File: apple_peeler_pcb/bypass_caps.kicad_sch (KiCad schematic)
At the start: 16 parts

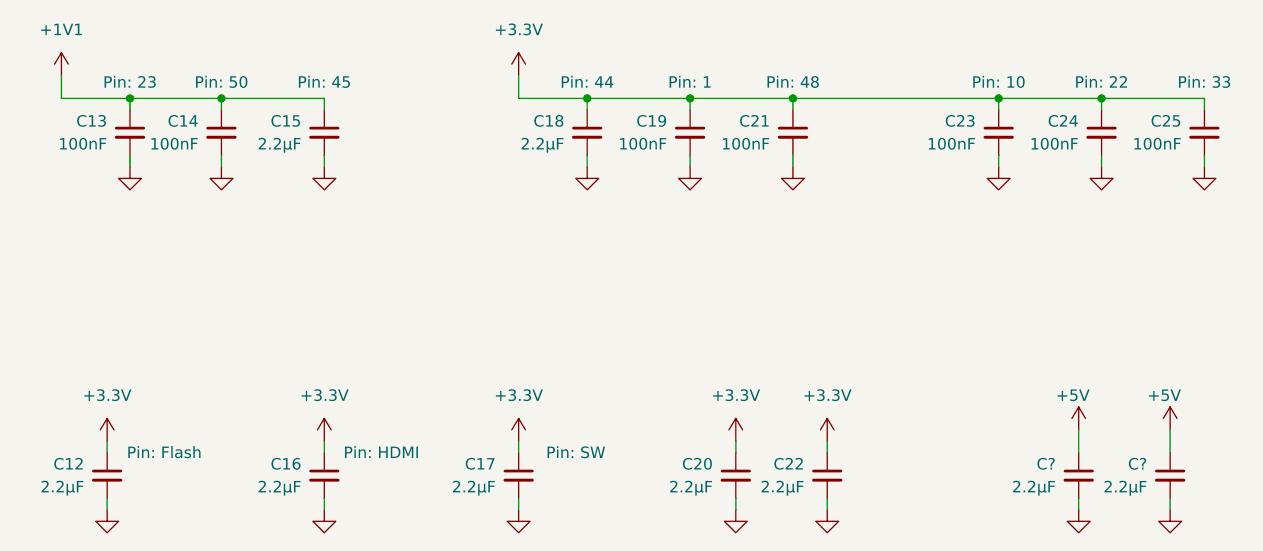
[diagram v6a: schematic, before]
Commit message: all components placed inside board
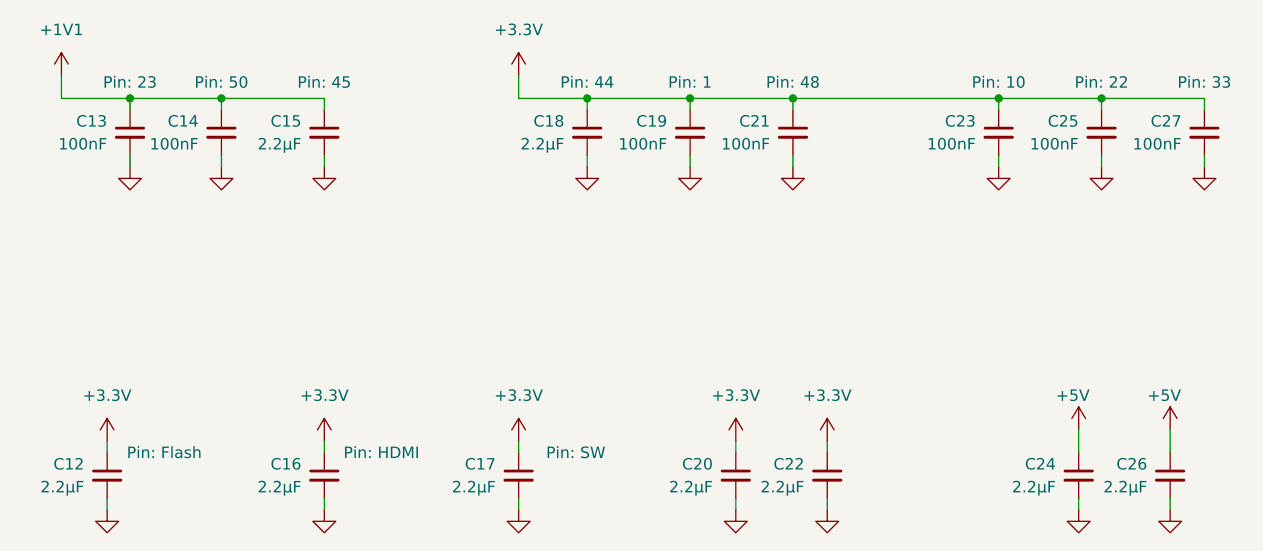
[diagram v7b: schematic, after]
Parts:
- gave numbers to parts that had none: 2
- renumbered C24 to C25, C25 to C27
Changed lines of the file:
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@@
 		(dnp no)
 		(fields_autoplaced yes)
-		(property "Reference" "#PWR086"
+		(property "Reference" "#PWR087"
 			(at 161.29 111.76 0)
 			(effects
@@
 			(project "apple_peeler_pcb"
 				(path "/d5946b96-44a8-4a28-8641-19803e1510af/36c29319-2fb9-4e97-8e03-94576ed291d6"
-					(reference "#PWR086")
+					(reference "#PWR087")
 					(unit 1)
 				)
@@
 		(dnp no)
 		(fields_autoplaced yes)
-		(property "Reference" "#PWR083"
+		(property "Reference" "#PWR084"
 			(at 151.13 111.76 0)
 			(effects
@@
 			(project "apple_peeler_pcb"
 				(path "/d5946b96-44a8-4a28-8641-19803e1510af/36c29319-2fb9-4e97-8e03-94576ed291d6"
-					(reference "#PWR083")
+					(reference "#PWR084")
 					(unit 1)
 				)
@@
 		(dnp no)
 		(fields_autoplaced yes)
-		(property "Reference" "#PWR081"
+		(property "Reference" "#PWR082"
 			(at 146.05 73.66 0)
 			(effects
@@
 			(project ""
 				(path "/d5946b96-44a8-4a28-8641-19803e1510af/36c29319-2fb9-4e97-8e03-94576ed291d6"
-					(reference "#PWR081")
+					(reference "#PWR082")
 					(unit 1)
 				)
@@
 		(dnp no)
 		(fields_autoplaced yes)
-		(property "Reference" "#PWR079"
+		(property "Reference" "#PWR080"
 			(at 127 111.76 0)
 			(effects
@@
 			(project "apple_peeler_pcb"
 				(path "/d5946b96-44a8-4a28-8641-19803e1510af/36c29319-2fb9-4e97-8e03-94576ed291d6"
-					(reference "#PWR079")
+					(reference "#PWR080")
 					(unit 1)
 				)
@@
 		(dnp no)
 		(fields_autoplaced yes)
-		(property "Reference" "#PWR0126"
+		(property "Reference" "#PWR093"
 			(at 199.39 111.76 0)
 			(effects
@@
 			(project "apple_peeler_pcb"
 				(path "/d5946b96-44a8-4a28-8641-19803e1510af/36c29319-2fb9-4e97-8e03-94576ed291d6"
-					(reference "#PWR0126")
+					(reference "#PWR093")
 					(unit 1)
 				)
@@
 		(dnp no)
 		(fields_autoplaced yes)
-		(property "Reference" "#PWR074"
+		(property "Reference" "#PWR075"
 			(at 105.41 73.66 0)
 			(effects
@@
 			(project ""
 				(path "/d5946b96-44a8-4a28-8641-19803e1510af/36c29319-2fb9-4e97-8e03-94576ed291d6"
-					(reference "#PWR074")
+					(reference "#PWR075")
 					(unit 1)
 				)
@@
 		(dnp no)
 		(fields_autoplaced yes)
-		(property "Reference" "#PWR080"
+		(property "Reference" "#PWR081"
 			(at 134.62 73.66 0)
 			(effects
@@
 			(project ""
 				(path "/d5946b96-44a8-4a28-8641-19803e1510af/36c29319-2fb9-4e97-8e03-94576ed291d6"
-					(reference "#PWR080")
+					(reference "#PWR081")
 					(unit 1)
 				)
@@
 		(dnp no)
 		(fields_autoplaced yes)
-		(property "Reference" "#PWR069"
+		(property "Reference" "#PWR070"
 			(at 76.2 60.96 0)
 			(effects
@@
 			(project ""
 				(path "/d5946b96-44a8-4a28-8641-19803e1510af/36c29319-2fb9-4e97-8e03-94576ed291d6"
-					(reference "#PWR069")
+					(reference "#PWR070")
 					(unit 1)
 				)
@@
 		(dnp no)
 		(fields_autoplaced yes)
-		(property "Reference" "#PWR077"
+		(property "Reference" "#PWR078"
 			(at 127 60.96 0)
 			(effects
@@
 			(project ""
 				(path "/d5946b96-44a8-4a28-8641-19803e1510af/36c29319-2fb9-4e97-8e03-94576ed291d6"
-					(reference "#PWR077")
+					(reference "#PWR078")
 					(unit 1)
 				)
@@
 		(dnp no)
 		(fields_autoplaced yes)
-		(property "Reference" "#PWR089"
+		(property "Reference" "#PWR094"
 			(at 203.2 73.66 0)
 			(effects
@@
 			(project ""
 				(path "/d5946b96-44a8-4a28-8641-19803e1510af/36c29319-2fb9-4e97-8e03-94576ed291d6"
-					(reference "#PWR089")
+					(reference "#PWR094")
 					(unit 1)
 				)
@@
 		(dnp no)
 		(fields_autoplaced yes)
-		(property "Reference" "#PWR072"
+		(property "Reference" "#PWR073"
 			(at 83.82 73.66 0)
 			(effects
@@
 			(project ""
 				(path "/d5946b96-44a8-4a28-8641-19803e1510af/36c29319-2fb9-4e97-8e03-94576ed291d6"
-					(reference "#PWR072")
+					(reference "#PWR073")
 					(unit 1)
 				)
@@
 		(on_board yes)
 		(dnp no)
-		(property "Reference" "#PWR0123"
+		(property "Reference" "#PWR089"
 			(at 189.23 100.33 0)
 			(effects
@@
 			(project "apple_peeler_pcb"
 				(path "/d5946b96-44a8-4a28-8641-19803e1510af/36c29319-2fb9-4e97-8e03-94576ed291d6"
-					(reference "#PWR0123")
+					(reference "#PWR089")
 					(unit 1)
 				)
@@
 		(dnp no)
 		(fields_autoplaced yes)
-		(property "Reference" "#PWR073"
+		(property "Reference" "#PWR074"
 			(at 93.98 73.66 0)
 			(effects
@@
 			(project ""
 				(path "/d5946b96-44a8-4a28-8641-19803e1510af/36c29319-2fb9-4e97-8e03-94576ed291d6"
-					(reference "#PWR073")
+					(reference "#PWR074")
 					(unit 1)
 				)
@@
 		(on_board yes)
 		(dnp no)
-		(property "Reference" "C24"
+		(property "Reference" "C25"
 			(at 189.23 62.2362 0)
 			(effects
@@
 			(project ""
 				(path "/d5946b96-44a8-4a28-8641-19803e1510af/36c29319-2fb9-4e97-8e03-94576ed291d6"
-					(reference "C24")
+					(reference "C25")
 					(unit 1)
 				)
@@
 		(dnp no)
 		(fields_autoplaced yes)
-		(property "Reference" "#PWR084"
+		(property "Reference" "#PWR085"
 			(at 157.48 73.66 0)
 			(effects
@@
 			(project ""
 				(path "/d5946b96-44a8-4a28-8641-19803e1510af/36c29319-2fb9-4e97-8e03-94576ed291d6"
-					(reference "#PWR084")
+					(reference "#PWR085")
 					(unit 1)
 				)
@@
 		(on_board yes)
 		(dnp no)
-		(property "Reference" "C?"
+		(property "Reference" "C24"
 			(at 186.69 100.3362 0)
 			(effects
@@
 			(project "apple_peeler_pcb"
 				(path "/d5946b96-44a8-4a28-8641-19803e1510af/36c29319-2fb9-4e97-8e03-94576ed291d6"
-					(reference "C?")
+					(reference "C24")
 					(unit 1)
 				)
@@
 		(dnp no)
 		(fields_autoplaced yes)
-		(property "Reference" "#PWR070"
+		(property "Reference" "#PWR071"
 			(at 81.28 101.6 0)
 			(effects
@@
 			(project "apple_peeler_pcb"
 				(path "/d5946b96-44a8-4a28-8641-19803e1510af/36c29319-2fb9-4e97-8e03-94576ed291d6"
-					(reference "#PWR070")
+					(reference "#PWR071")
 					(unit 1)
 				)
@@
 		(dnp no)
 		(fields_autoplaced yes)
-		(property "Reference" "#PWR087"
+		(property "Reference" "#PWR088"
 			(at 180.34 73.66 0)
 			(effects
@@
 			(project ""
 				(path "/d5946b96-44a8-4a28-8641-19803e1510af/36c29319-2fb9-4e97-8e03-94576ed291d6"
-					(reference "#PWR087")
+					(reference "#PWR088")
 					(unit 1)
 				)
@@
 		(on_board yes)
 		(dnp no)
-		(property "Reference" "C25"
+		(property "Reference" "C27"
 			(at 200.66 62.2362 0)
 			(effects
@@
 			(project ""
 				(path "/d5946b96-44a8-4a28-8641-19803e1510af/36c29319-2fb9-4e97-8e03-94576ed291d6"
-					(reference "C25")
+					(reference "C27")
 					(unit 1)
 				)
@@
 		(dnp no)
 		(fields_autoplaced yes)
-		(property "Reference" "#PWR075"
+		(property "Reference" "#PWR076"
 			(at 105.41 101.6 0)
 			(effects
@@
 			(project "apple_peeler_pcb"
 				(path "/d5946b96-44a8-4a28-8641-19803e1510af/36c29319-2fb9-4e97-8e03-94576ed291d6"
-					(reference "#PWR075")
+					(reference "#PWR076")
 					(unit 1)
 				)
@@
 		(dnp no)
 		(fields_autoplaced yes)
-		(property "Reference" "#PWR071"
+		(property "Reference" "#PWR072"
 			(at 81.28 111.76 0)
 			(effects
@@
 			(project "apple_peeler_pcb"
 				(path "/d5946b96-44a8-4a28-8641-19803e1510af/36c29319-2fb9-4e97-8e03-94576ed291d6"
-					(reference "#PWR071")
+					(reference "#PWR072")
 					(unit 1)
 				)
@@
 		(dnp no)
 		(fields_autoplaced yes)
-		(property "Reference" "#PWR078"
+		(property "Reference" "#PWR079"
 			(at 127 101.6 0)
 			(effects
@@
 			(project "apple_peeler_pcb"
 				(path "/d5946b96-44a8-4a28-8641-19803e1510af/36c29319-2fb9-4e97-8e03-94576ed291d6"
-					(reference "#PWR078")
+					(reference "#PWR079")
 					(unit 1)
 				)
@@
 		(dnp no)
 		(fields_autoplaced yes)
-		(property "Reference" "#PWR088"
+		(property "Reference" "#PWR091"
 			(at 191.77 73.66 0)
 			(effects
@@
 			(project ""
 				(path "/d5946b96-44a8-4a28-8641-19803e1510af/36c29319-2fb9-4e97-8e03-94576ed291d6"
-					(reference "#PWR088")
+					(reference "#PWR091")
 					(unit 1)
 				)
@@
 		(on_board yes)
 		(dnp no)
-		(property "Reference" "C?"
+		(property "Reference" "C26"
 			(at 196.85 100.3362 0)
 			(effects
@@
 			(project "apple_peeler_pcb"
 				(path "/d5946b96-44a8-4a28-8641-19803e1510af/36c29319-2fb9-4e97-8e03-94576ed291d6"
-					(reference "C?")
+					(reference "C26")
 					(unit 1)
 				)
@@
 		(dnp no)
 		(fields_autoplaced yes)
-		(property "Reference" "#PWR0124"
+		(property "Reference" "#PWR090"
 			(at 189.23 111.76 0)
 			(effects
@@
 			(project "apple_peeler_pcb"
 				(path "/d5946b96-44a8-4a28-8641-19803e1510af/36c29319-2fb9-4e97-8e03-94576ed291d6"
-					(reference "#PWR0124")
+					(reference "#PWR090")
 					(unit 1)
 				)
@@
 		(dnp no)
 		(fields_autoplaced yes)
-		(property "Reference" "#PWR085"
+		(property "Reference" "#PWR086"
 			(at 161.29 101.6 0)
 			(effects
@@
 			(project "apple_peeler_pcb"
 				(path "/d5946b96-44a8-4a28-8641-19803e1510af/36c29319-2fb9-4e97-8e03-94576ed291d6"
-					(reference "#PWR085")
+					(reference "#PWR086")
 					(unit 1)
 				)
@@
 		(dnp no)
 		(fields_autoplaced yes)
-		(property "Reference" "#PWR076"
+		(property "Reference" "#PWR077"
 			(at 105.41 111.76 0)
 			(effects
@@
 			(project "apple_peeler_pcb"
 				(path "/d5946b96-44a8-4a28-8641-19803e1510af/36c29319-2fb9-4e97-8e03-94576ed291d6"
-					(reference "#PWR076")
+					(reference "#PWR077")
 					(unit 1)
 				)
@@
 		(dnp no)
 		(fields_autoplaced yes)
-		(property "Reference" "#PWR082"
+		(property "Reference" "#PWR083"
 			(at 151.13 101.6 0)
 			(effects
@@
 			(project "apple_peeler_pcb"
 				(path "/d5946b96-44a8-4a28-8641-19803e1510af/36c29319-2fb9-4e97-8e03-94576ed291d6"
-					(reference "#PWR082")
+					(reference "#PWR083")
 					(unit 1)
 				)
@@
 		(on_board yes)
 		(dnp no)
-		(property "Reference" "#PWR0125"
+		(property "Reference" "#PWR092"
 			(at 199.39 100.33 0)
 			(effects
@@
 			(project "apple_peeler_pcb"
 				(path "/d5946b96-44a8-4a28-8641-19803e1510af/36c29319-2fb9-4e97-8e03-94576ed291d6"
-					(reference "#PWR0125")
-					(unit 1)
-				)
+					(reference "#PWR092")
+					(unit 1)
+				)

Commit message: copper seems done, only thing left is the silkscreen
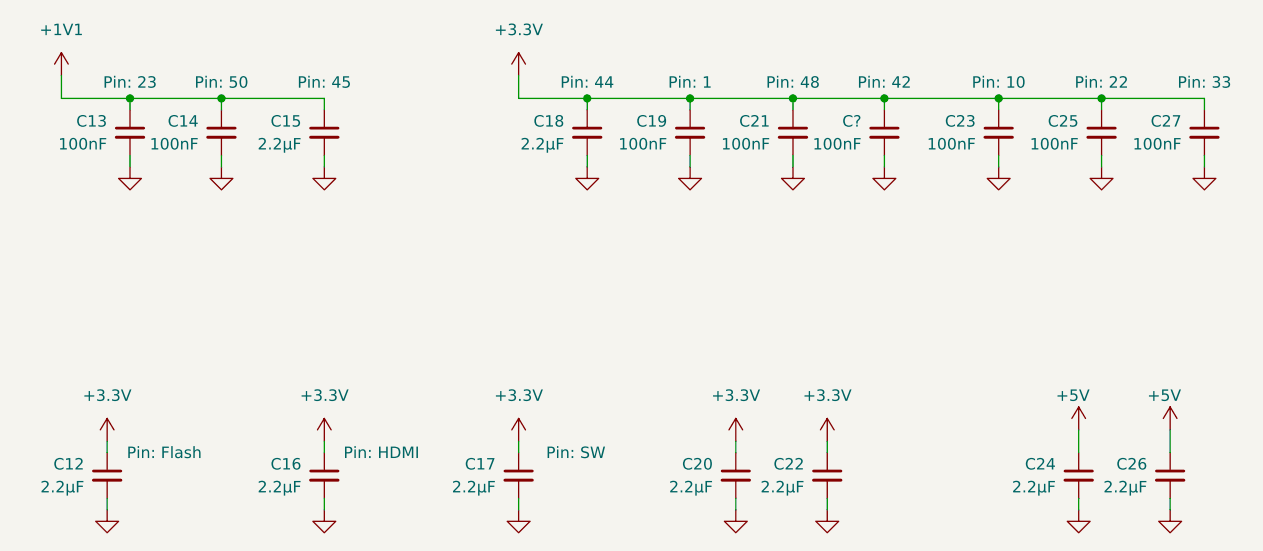
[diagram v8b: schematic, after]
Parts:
- added C?: 100nF, Capacitor_SMD:C_0805_2012Metric, symbol Device:C_Small
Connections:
- net +3.3V: now also C?.1
- net GND: now also C?.2
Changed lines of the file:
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@@
 	)
 	(junction
+		(at 167.64 59.69)
+		(diameter 0)
+		(color 0 0 0 0)
+	)
+	(junction
 		(at 191.77 59.69)
 		(diameter 0)
@@
 	(wire
 		(pts
-			(xy 157.48 59.69) (xy 180.34 59.69)
+			(xy 157.48 59.69) (xy 167.64 59.69)
 		)
 		(stroke
@@
 	(wire
 		(pts
+			(xy 167.64 59.69) (xy 180.34 59.69)
+		)
+		(stroke
+			(width 0)
+			(type default)
+		)
+	)
+	(wire
+		(pts
 			(xy 199.39 104.14) (xy 199.39 105.41)
 		)
@@
 	(wire
 		(pts
+			(xy 167.64 66.04) (xy 167.64 67.31)
+		)
+		(stroke
+			(width 0)
+			(type default)
+		)
+	)
+	(wire
+		(pts
 			(xy 180.34 66.04) (xy 180.34 67.31)
 		)
@@
 	(wire
 		(pts
+			(xy 167.64 59.69) (xy 167.64 60.96)
+		)
+		(stroke
+			(width 0)
+			(type default)
+		)
+	)
+	(wire
+		(pts
 			(xy 127 57.15) (xy 127 59.69)
 		)
@@
 	)
 	(symbol
+		(lib_id "power:GND")
+		(at 167.64 67.31 0)
+		(unit 1)
+		(exclude_from_sim no)
+		(in_bom yes)
+		(on_board yes)
+		(dnp no)
+		(fields_autoplaced yes)
+		(property "Reference" "#PWR0127"
+			(at 167.64 73.66 0)
+			(effects
+				(font
+					(size 1.27 1.27)
+				)
+				(hide yes)
+			)
+		)
+		(property "Value" "GND"
+			(at 167.64 72.39 0)
+			(effects
+				(font
+					(size 1.27 1.27)
+				)
+				(hide yes)
+			)
+		)
+		(property "Footprint" ""
+			(at 167.64 67.31 0)
+			(effects
+				(font
+					(size 1.27 1.27)
+				)
+				(hide yes)
+			)
+		)
+		(property "Datasheet" ""
+			(at 167.64 67.31 0)
+			(effects
+				(font
+					(size 1.27 1.27)
+				)
+				(hide yes)
+			)
+		)
+		(property "Description" "Power symbol creates a global label with name \"GND\" , ground"
+			(at 167.64 67.31 0)
+			(effects
+				(font
+					(size 1.27 1.27)
+				)
+				(hide yes)
+			)
+		)
+		(pin "1"
+		)
+		(instances
+			(project "apple_peeler_pcb"
+				(path "/d5946b96-44a8-4a28-8641-19803e1510af/36c29319-2fb9-4e97-8e03-94576ed291d6"
+					(reference "#PWR0127")
+					(unit 1)
+				)
+			)
+		)
+	)
+	(symbol
 		(lib_id "Device:C_Small")
 		(at 151.13 101.6 0)
@@
 					(unit 1)
 				)
+			)
+		)
+	)
+	(symbol
+		(lib_id "Device:C_Small")
+		(at 167.64 63.5 0)
+		(mirror y)
+		(unit 1)
+		(exclude_from_sim no)
+		(in_bom yes)
+		(on_board yes)
+		(dnp no)
+		(property "Reference" "C?"
+			(at 165.1 62.2362 0)
+			(effects
+				(font
+					(size 1.27 1.27)
+				)
+				(justify left)
+			)
+		)
+		(property "Value" "100nF"
+			(at 165.1 64.7762 0)
+			(effects
+				(font
+					(size 1.27 1.27)
+				)
+				(justify left)
+			)
+		)
+		(property "Footprint" "Capacitor_SMD:C_0805_2012Metric"
+			(at 167.64 63.5 0)
+			(effects
+				(font
+					(size 1.27 1.27)
+				)
+				(hide yes)
+			)
+		)
+		(property "Datasheet" "~"
+			(at 167.64 63.5 0)
+			(effects
+				(font
+					(size 1.27 1.27)
+				)
+				(hide yes)
+			)
+		)
+		(property "Description" "Unpolarized capacitor, small symbol"
+			(at 167.64 63.5 0)
+			(effects
+				(font
+					(size 1.27 1.27)
+				)
+				(hide yes)
+			)
+		)
+		(property "LCSC" "C49678"
+			(at 167.64 63.5 0)
+			(effects
+				(font
+					(size 1.27 1.27)
+				)
+				(hide yes)
+			)
+		)
+		(property "MPN" "C 100nF 50V 0805"
+			(at 167.64 63.5 0)
+			(effects
+				(font
+					(size 1.27 1.27)
+				)
+				(hide yes)
+			)
+		)
+		(property "Pin" "42"
+			(at 167.64 57.912 0)
+			(show_name yes)
+			(effects
+				(font
+					(size 1.27 1.27)
+				)
+			)
+		)
+		(pin "2"
+		)
+		(pin "1"
+		)
+		(instances
+			(project "apple_peeler_pcb"
+				(path "/d5946b96-44a8-4a28-8641-19803e1510af/36c29319-2fb9-4e97-8e03-94576ed291d6"
+					(reference "C?")
+					(unit 1)
+				)
